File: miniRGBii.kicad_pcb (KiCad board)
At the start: 2 copper layers, 30 x 15 mm, 28 parts, among them J1 Conn_01x01_Male, J2 Conn_01x01_Male, J3 Conn_01x01_Male, J4 Conn_01x01_Male, J5 Conn_01x01_Male, J6 Conn_01x01_Male, J7 Conn_01x01_Male, J8 Conn_01x01_Male, J9 Conn_01x01_Male

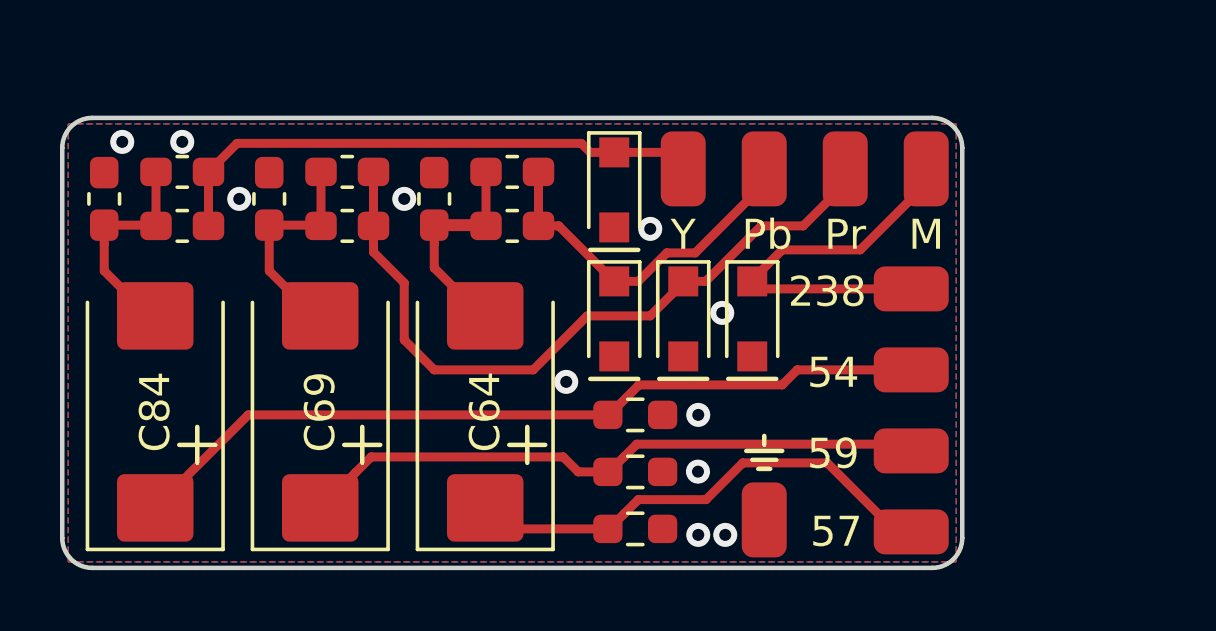
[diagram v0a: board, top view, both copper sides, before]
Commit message: Change cap footprint to reduce board size
Signed-off-by: Devnol <pgkoutsoumanis@gmail.com>
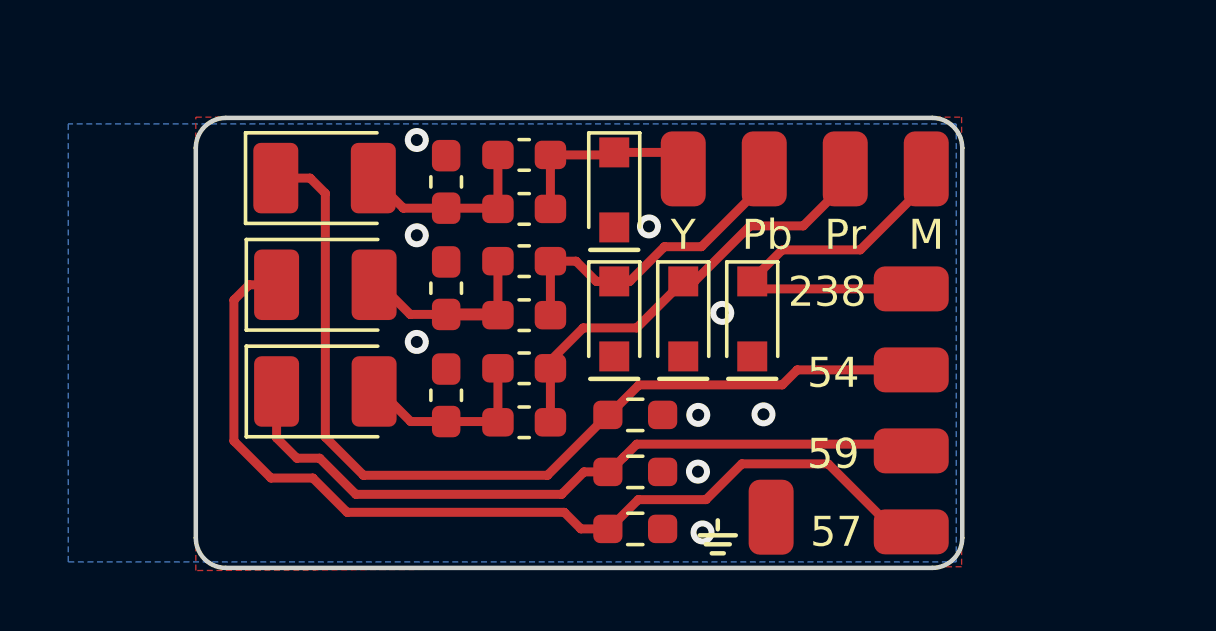
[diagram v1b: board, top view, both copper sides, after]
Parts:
- C64, C69, C84: footprint Capacitor_Tantalum_SMD:CP_EIA-7343-15_Kemet-W_Pad2.25x2.55mm_HandSolder -> Capacitor_Tantalum_SMD:CP_EIA-3528-12_Kemet-T_Pad1.50x2.35mm_HandSolder
- moved C83 11.4 mm to (198.4, 55.2)
- moved C85 11.4 mm to (195.8, 56.1)
- moved FIL17 11.4 mm to (198.4, 57.0)
- moved C84 9.62 mm to (191.7, 56.0), turned to 0 degrees
- moved C66 8.81 mm to (198.4, 62.3)
- moved C72 8.81 mm to (195.8, 63.2)
- moved FIL15 8.81 mm to (198.4, 64.1)
- moved C64 6.81 mm to (191.8, 59.6), turned to 0 degrees
- moved C74 3.00 mm to (198.4, 58.8)
- moved C78 3.00 mm to (195.8, 59.7)
- moved FIL16 3.00 mm to (198.4, 60.6)
- moved C69 0.70 mm to (191.8, 63.1), turned to 0 degrees
- moved J9 0.25 mm to (206.6, 67.3), turned to 0 degrees
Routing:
- net AVE57: track 16.5 -> 32.1 mm
- net YOut: track 18.4 -> 6.49 mm
- net PrOut: track 24.2 -> 14.8 mm
- net AVE54: track 27.1 -> 31.2 mm
- net AVE59: track 21.1 -> 24.0 mm
- net Net-(C66-Pad1): track 7.48 -> 6.14 mm
- net Net-(C64-Pad2): track 7.32 -> 6.13 mm
- net Net-(C83-Pad1): track 7.38 -> 6.38 mm
- net PbOut: track 12.0 -> 11.1 mm
- net GND: vias 11 -> 9
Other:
- board size 30 x 15 mm -> 25.5 x 15 mm

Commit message: Generate output files and add fab documentation
Signed-off-by: Devnol <pgkoutsoumanis@gmail.com>
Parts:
- moved D3 6.59 mm to (210.1, 58.9)
- moved J1 6.59 mm to (210.1, 53.9)
- moved J9 6.59 mm to (213.0, 65.5)
- moved C64 6.59 mm to (198.1, 57.8)
- moved C74 6.59 mm to (204.7, 57.0)
- moved D2 6.59 mm to (207.8, 58.9)
- moved D4 6.59 mm to (212.3, 58.9)
- moved J2 6.59 mm to (212.8, 53.9)
- moved J3 6.59 mm to (215.4, 53.9)
- moved J4 6.59 mm to (217.7, 57.9)
- moved J5 6.59 mm to (218.2, 53.9)
- moved R39 6.59 mm to (208.4, 65.9)
- moved C66 6.59 mm to (204.7, 60.6)
- moved C69 6.59 mm to (198.1, 61.3)
- moved C72 6.59 mm to (202.1, 61.5)
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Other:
- board text added: "bit.ly/miniRGBii"
- board text removed: "discord.gg/7jNHphfDQk"
